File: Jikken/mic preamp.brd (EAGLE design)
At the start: 100 x 80 mm, 13 parts

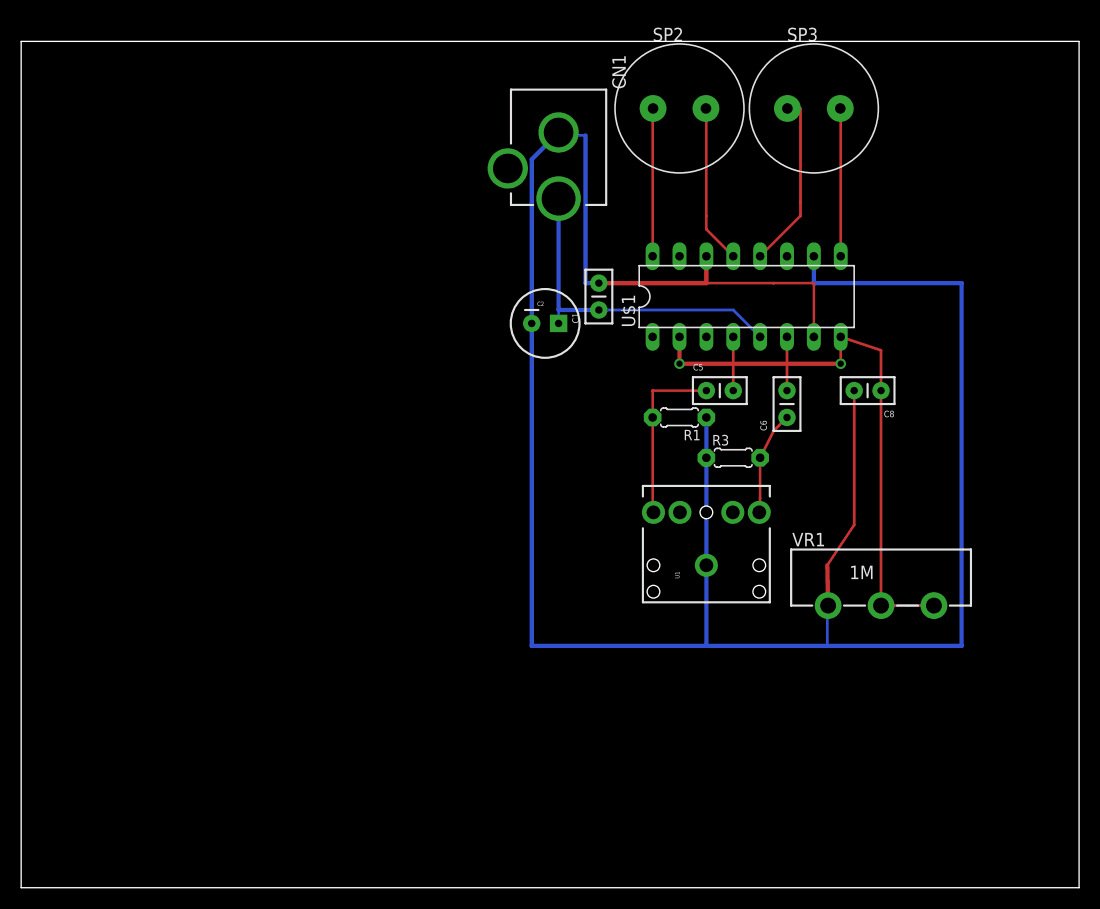
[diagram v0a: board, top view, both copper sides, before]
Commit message: TDA7053 Stereo Audio Power Amplifier
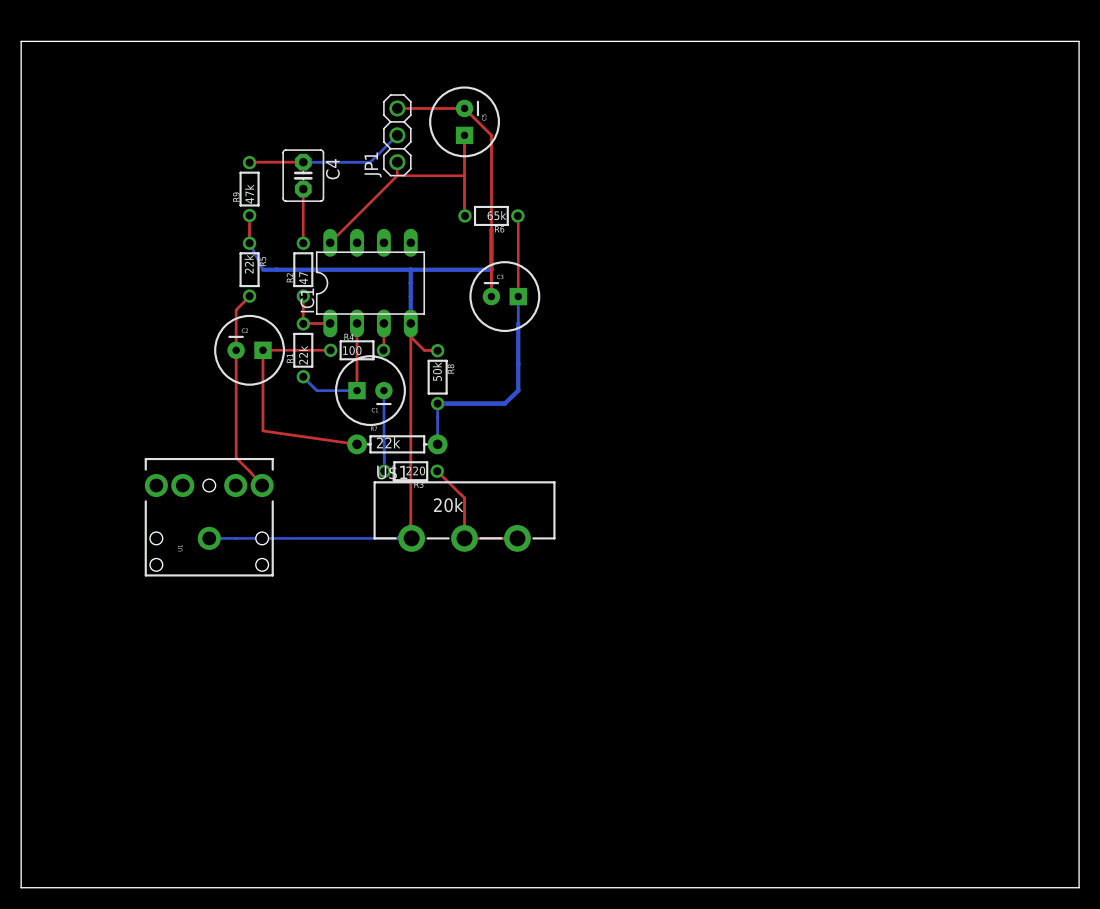
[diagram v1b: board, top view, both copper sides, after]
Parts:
- removed C6: 0.47u, SparkFun:CAP-PTH-SMALL2
- removed C8: 0.1u, SparkFun:CAP-PTH-SMALL2
- removed CN1: (no value), adafruit:DCJACK_2MM_PTH
- removed SP2, SP3: SP, My Library:PS12
- removed VR1: 1M, My Library:POT_ALPHA_RV16AF-20
- added C3: 10u, SparkFun:CPOL-RADIAL-100UF-25V
- added C4: 100u, capacitor-wima:C2.5-4
- added IC1: AD822N, analog-devices:DIL08
- added JP1: (no value), adafruit:1X03
- added R2: 47, My Library:1/6W-RES
- added R4: 100, My Library:1/6W-RES
- added R5: 22k, My Library:1/6W-RES
- added R6: 65k, My Library:1/6W-RES
- added R7: 22k, My Library:AXIAL-0.3
- added R8: 50k, My Library:1/6W-RES
- added R9: 47k, My Library:1/6W-RES
- C1: value 0.1u -> 100u; device SparkFun:CAP-PTH-SMALL2 -> SparkFun:CPOL-RADIAL-100UF-25V
- C2: value 220u -> 100u
- C5: value 0.47u -> 100u; device SparkFun:CAP-PTH-SMALL2 -> SparkFun:CPOL-RADIAL-100UF-25V
- R1: value 4k7 -> 22k; device adafruit:0204/5 -> My Library:1/6W-RES
- R3: value 4k7 -> 220; device adafruit:0204/5 -> My Library:1/6W-RES
- U$1: value TDA7053A -> 20k; device My Library:DIL16 -> My Library:POT_ALPHA_RV16AF-20
- moved U1 47.1 mm to (17.8, 33.0)
- moved R1 36.1 mm to (26.7, 50.8), turned to 90 degrees
- moved U$1 35.1 mm to (41.9, 33.0)
- moved C5 34.2 mm to (41.9, 72.4), turned to 270 degrees
- moved R3 30.5 mm to (36.8, 39.4), turned to 180 degrees
- moved C2 28.1 mm to (21.6, 50.8)
- moved C1 22.9 mm to (33.0, 47.0), turned to 180 degrees
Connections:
- removed net GNDBREAK: CN1.GNDBREAK
- removed net N$10: SP3.P$1, U$1.12
- removed net N$11: SP2.P$2, U$1.13
- removed net N$12: SP2.P$1, U$1.16
- removed net N$14: C6.2, U$1.6
- removed net N$15: C5.2, U$1.4
- removed net N$17: C1.1, C2.1, CN1.PWR, U$1.5
- removed net N$19: C8.1, U$1.2, U$1.8, VR1.2, VR1.3
- new net N$1: R3.1, U$1.2, U$1.3
- new net N$13: C4.1, JP1.2, R9.2
- new net N$2: C1.2, R3.2
- new net N$3: IC1.1, R1.2, R2.1
- new net N$5: C1.1, IC1.2, R1.1
- new net N$8: IC1.3, R4.2
- new net N$9: C3.1, R6.1, R7.P$2, R8.2
- new net VCC: C5.1, IC1.8, JP1.1, R6.2
- net GND: now also C3.2, C5.2, IC1.4, JP1.3, R5.1, R8.1, R9.1, U$1.1; no longer C1.2, C2.2, C8.2, CN1.GND, R1.1, R3.1, U$1.10, U$1.14, U$1.7, VR1.1
- net N$4: now also C4.2, R2.2; no longer C5.1, R1.2, U1.RING
- net N$6: now also C2.2, R5.2; no longer C6.1, R3.2
- net N$7: now also C2.1, R4.1, R7.P$1; no longer SP3.P$2, U$1.9
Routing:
- net GND: track 240.0 -> 107.9 mm
- net N$19: track 53.5 -> 0.00 mm, vias 2 -> 0
- net N$17: track 31.9 -> 0.00 mm
- net N$9: track 0.00 -> 28.5 mm
- net VCC: track 0.00 -> 24.3 mm
- net N$10: track 16.8 -> 0.00 mm
- net N$13: track 0.00 -> 15.1 mm
- net N$11: track 15.1 -> 0.00 mm
- net N$12: track 14.0 -> 0.00 mm
- net N$1: track 0.00 -> 12.4 mm
- net N$5: track 0.00 -> 12.0 mm
- net N$4: track 16.6 -> 5.12 mm
- net N$6: track 9.80 -> 19.4 mm
- net N$7: track 14.0 -> 23.0 mm
- net N$2: track 0.00 -> 7.62 mm
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
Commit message: jikken
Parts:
- removed JP1: (no value), adafruit:1X03
- added C6, C8: 100u, SparkFun:CPOL-RADIAL-100UF-25V
- added C7: 100u, capacitor-wima:C2.5-4
- added JP2: (no value), SparkFun:MOLEX-1X4
- added R10: 47, My Library:1/6W-RES
- added R11, R15: 22k, My Library:1/6W-RES
- added R12: 220, My Library:1/6W-RES
- added R13: 47k, My Library:1/6W-RES
- added R14: 100, My Library:1/6W-RES
- added R16: 22k, My Library:AXIAL-0.3
- added U$2: 20k, My Library:POT_ALPHA_RV16AF-20
- R6: value 65k -> 68k
- R8: value 50k -> 47k
- moved C4 24.4 mm to (15.2, 45.7), turned to 0 degrees
- moved R9 22.7 mm to (11.4, 45.7), turned to 270 degrees
- moved C5 19.1 mm to (43.2, 53.3), turned to 180 degrees
- moved R2 13.0 mm to (24.1, 45.7), turned to 180 degrees
- moved R5 13.0 mm to (19.1, 45.7)
- moved C2 11.5 mm to (20.3, 39.4)
- moved R1 10.2 mm to (26.7, 40.6)
- moved U1 9.67 mm to (8.89, 29.2), turned to 0 degrees
- moved U$1 9.25 mm to (50.8, 30.5), turned to 90 degrees
- moved C1 8.89 mm to (33.0, 38.1)
- moved C3 8.89 mm to (45.7, 47.0)
- moved R3 8.89 mm to (36.8, 30.5)
- moved R7 8.89 mm to (35.6, 33.0)
- moved IC1 7.62 mm to (33.0, 49.5)
- moved R4 7.62 mm to (31.8, 43.2)
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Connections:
- new net N$10: R12.1, U$2.2, U$2.3
- new net N$11: C6.2, R12.2
- new net N$12: C6.1, IC1.6, R11.1
- new net N$14: IC1.7, R10.1, R11.2
- new net N$15: C8.2, R15.2, U1.RING
- new net N$16: C7.2, R10.2
- new net N$17: C7.1, JP2.3, R13.2
- new net N$18: C8.1, R14.1, R16.P$1
- new net N$19: IC1.5, R14.2
- net GND: now also JP2.1, R13.1, R15.1, U$2.1; no longer JP1.3
- net N$13: now also JP2.2; no longer JP1.2
- net N$9: now also R16.P$2
- net VCC: now also JP2.4; no longer JP1.1
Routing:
- net N$15: track 0.00 -> 44.5 mm
- net N$6: track 19.4 -> 39.5 mm
- net GND: track 107.9 -> 122.5 mm
- net N$13: track 15.1 -> 5.08 mm
- net N$9: track 28.5 -> 20.9 mm
- net N$3: track 5.20 -> 0.00 mm
- net N$1: track 12.4 -> 16.5 mm
- net N$7: track 23.0 -> 25.7 mm
- net VCC: track 24.3 -> 22.9 mm
- net N$5: track 12.0 -> 12.7 mm
